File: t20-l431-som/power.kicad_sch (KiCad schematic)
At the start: 21 parts, among them U1 STM32L431-WLCSP64, U2 T20W80

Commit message: Continued initial work on t20-l431 som
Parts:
- added C18: 1 uF, azonenberg_pcb:EIA_0201_CAP_NOSILK, symbol device:C
- C1, C10, C11, C12, C13, C14, C15, C16, C17, C2, C3, C4, C5, C6, C7, C8, C9, L1, L2: footprint (none) -> azonenberg_pcb:EIA_0201_CAP_NOSILK
- U1: footprint (none) -> azonenberg_pcb:BGA_64_0.35MM_3p1MM_STM32L431
- U2: footprint (none) -> azonenberg_pcb:BGA_80_0.4MM_4p4x3p5_T20W80
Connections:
- net A1V2_PLL: now also C18.1
- net GND: now also C18.2
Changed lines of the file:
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@@
 	(generator "eeschema")
 	(generator_version "9.0")
-	(paper "A3")
+	(paper "A4")
 	(text "TODO: LDOs"
 		(exclude_from_sim no)
@@
 	)
 	(junction
+		(at 92.71 99.06)
+		(diameter 0)
+		(color 0 0 0 0)
+	)
+	(junction
 		(at 26.67 30.48)
 		(diameter 0)
@@
 	(wire
 		(pts
+			(xy 92.71 99.06) (xy 105.41 99.06)
+		)
+		(stroke
+			(width 0)
+			(type default)
+		)
+	)
+	(wire
+		(pts
 			(xy 26.67 76.2) (xy 26.67 78.74)
 		)
@@
 		(pts
 			(xy 26.67 78.74) (xy 26.67 81.28)
+		)
+		(stroke
+			(width 0)
+			(type default)
+		)
+	)
+	(wire
+		(pts
+			(xy 92.71 106.68) (xy 105.41 106.68)
 		)
 		(stroke
@@
 			)
 			(justify right bottom)
+		)
+	)
+	(hierarchical_label "1V8"
+		(shape output)
+		(at 151.13 64.77 0)
+		(effects
+			(font
+				(size 1.27 1.27)
+			)
+			(justify left)
 		)
 	)
@@
 			)
 		)
-		(property "Footprint" ""
+		(property "Footprint" "azonenberg_pcb:EIA_0201_CAP_NOSILK"
 			(at 60.6552 67.31 0)
 			(effects
@@
 			)
 		)
-		(property "Footprint" ""
+		(property "Footprint" "azonenberg_pcb:BGA_64_0.35MM_3p1MM_STM32L431"
 			(at 30.48 49.53 0)
 			(effects
@@
 			)
 		)
-		(property "Footprint" ""
+		(property "Footprint" "azonenberg_pcb:EIA_0201_CAP_NOSILK"
 			(at 74.6252 67.31 0)
 			(effects
@@
 			)
 		)
-		(property "Footprint" ""
+		(property "Footprint" "azonenberg_pcb:EIA_0201_CAP_NOSILK"
 			(at 117.8052 81.28 0)
 			(effects
@@
 			)
 		)
-		(property "Footprint" ""
+		(property "Footprint" "azonenberg_pcb:EIA_0201_CAP_NOSILK"
 			(at 86.0552 67.31 0)
 			(effects
@@
 			)
 		)
-		(property "Footprint" ""
+		(property "Footprint" "azonenberg_pcb:EIA_0201_CAP_NOSILK"
 			(at 83.5152 46.99 0)
 			(effects
@@
 			)
 		)
-		(property "Footprint" ""
+		(property "Footprint" "azonenberg_pcb:EIA_0201_CAP_NOSILK"
 			(at 60.6552 81.28 0)
 			(effects
@@
 			)
 		)
-		(property "Footprint" ""
+		(property "Footprint" "azonenberg_pcb:EIA_0201_CAP_NOSILK"
 			(at 94.9452 81.28 0)
 			(effects
@@
 			)
 		)
-		(property "Footprint" ""
+		(property "Footprint" "azonenberg_pcb:EIA_0201_CAP_NOSILK"
 			(at 83.5152 81.28 0)
 			(effects
@@
 			)
 		)
-		(property "Footprint" ""
+		(property "Footprint" "azonenberg_pcb:EIA_0201_CAP_NOSILK"
 			(at 60.6552 93.98 0)
 			(effects
@@
 			)
 		)
-		(property "Footprint" ""
+		(property "Footprint" "azonenberg_pcb:BGA_80_0.4MM_4p4x3p5_T20W80"
 			(at 30.48 125.73 0)
 			(effects
@@
 				(path "/c9028163-a5a7-4e78-bba9-fb79df7846cd/cee616b2-310c-4168-8c64-88604d0390f4"
 					(reference "U2")
+					(unit 1)
+				)
+			)
+		)
+	)
+	(symbol
+		(lib_id "device:C")
+		(at 105.41 102.87 0)
+		(unit 1)
+		(exclude_from_sim no)
+		(in_bom yes)
+		(on_board yes)
+		(dnp no)
+		(fields_autoplaced yes)
+		(property "Reference" "C18"
+			(at 108.331 101.6578 0)
+			(effects
+				(font
+					(size 1.27 1.27)
+				)
+				(justify left)
+			)
+		)
+		(property "Value" "1 uF"
+			(at 108.331 104.0821 0)
+			(effects
+				(font
+					(size 1.27 1.27)
+				)
+				(justify left)
+			)
+		)
+		(property "Footprint" "azonenberg_pcb:EIA_0201_CAP_NOSILK"
+			(at 106.3752 106.68 0)
+			(effects
+				(font
+					(size 1.27 1.27)
+				)
+				(hide yes)
+			)
+		)
+		(property "Datasheet" ""
+			(at 105.41 102.87 0)
+			(effects
+				(font
+					(size 1.27 1.27)
+				)
+				(hide yes)
+			)
+		)
+		(property "Description" "Unpolarized capacitor"
+			(at 105.41 102.87 0)
+			(effects
+				(font
+					(size 1.27 1.27)
+				)
+				(hide yes)
+			)
+		)
+		(property "MPN" "GRM033C80J105ME05D"
+			(at 105.41 102.87 0)
+			(effects
+				(font
+					(size 1.27 1.27)
+				)
+				(hide yes)
+			)
+		)
+		(pin "2"
+		)
+		(pin "1"
+		)
+		(instances
+			(project "t20-l431-som"
+				(path "/c9028163-a5a7-4e78-bba9-fb79df7846cd/cee616b2-310c-4168-8c64-88604d0390f4"
+					(reference "C18")
 					(unit 1)
 				)
@@
 			)
 		)
-		(property "Footprint" ""
+		(property "Footprint" "azonenberg_pcb:EIA_0201_CAP_NOSILK"
 			(at 76.2 99.06 0)
 			(effects
@@
 					(size 1.524 1.524)
 				)
+				(hide yes)
 			)
 		)
@@
 			)
 		)
-		(property "Footprint" ""
+		(property "Footprint" "azonenberg_pcb:EIA_0201_CAP_NOSILK"
 			(at 72.0852 81.28 0)
 			(effects
@@
 			)
 		)
-		(property "Footprint" ""
+		(property "Footprint" "azonenberg_pcb:EIA_0201_CAP_NOSILK"
 			(at 97.4852 67.31 0)
 			(effects
@@
 			)
 		)
-		(property "Footprint" ""
+		(property "Footprint" "azonenberg_pcb:EIA_0201_CAP_NOSILK"
 			(at 72.0852 46.99 0)
 			(effects
@@
 			)
 		)
-		(property "Footprint" ""
+		(property "Footprint" "azonenberg_pcb:EIA_0201_CAP_NOSILK"
 			(at 106.3752 81.28 0)
 			(effects
@@
 			)
 		)
-		(property "Footprint" ""
+		(property "Footprint" "azonenberg_pcb:EIA_0201_CAP_NOSILK"
 			(at 93.6752 34.29 0)
 			(effects
@@
 			)
 		)
-		(property "Footprint" ""
+		(property "Footprint" "azonenberg_pcb:EIA_0201_CAP_NOSILK"
 			(at 93.6752 106.68 0)
 			(effects
@@
 			)
 		)
-		(property "Footprint" ""
+		(property "Footprint" "azonenberg_pcb:EIA_0201_CAP_NOSILK"
 			(at 93.6752 46.99 0)
 			(effects
@@
 			)
 		)
-		(property "Footprint" ""
+		(property "Footprint" "azonenberg_pcb:EIA_0201_CAP_NOSILK"
 			(at 60.6552 46.99 0)
 			(effects
@@
 			)
 		)
-		(property "Footprint" ""
+		(property "Footprint" "azonenberg_pcb:EIA_0201_CAP_NOSILK"
 			(at 76.2 26.67 0)
 			(effects
@@
 					(size 1.524 1.524)
 				)
-			)
-		)
+				(hide yes)
+			)
+		)

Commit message: Continued initial layout
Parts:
- added C20: 0.01 uF, azonenberg_pcb:EIA_0201_CAP_NOSILK, symbol device:C
- added C21, C22, C23: 1 uF, azonenberg_pcb:EIA_0201_CAP_NOSILK, symbol device:C
- added R2, R3: 10K, azonenberg_pcb:EIA_0201_RES_NOSILK, symbol device:R
- added U4: MODULE_INTERNAL_T20_L431_HOST, azonenberg_pcb:MODULE_INTERNAL_T20_L431_HOST, symbol special-azonenberg:MODULE_INTERNAL_T20_L431_HOST
- added U5: LP3986TL-2518/NOPB, azonenberg_pcb:BGA_8_0.5MM_1.6MM_TI_YZR0008, symbol power-azonenberg:LP3986
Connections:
- net 1V2: now also U4.C2 (1V2), U4.C3 (1V2), U4.D2 (1V2), U4.E2 (1V2), U4.F2 (1V2), U4.G4 (1V2)
- net 1V8: now also C21.1, U5.A1 (VOUT2)
- net 2V5: now also C22.1, U4.C4 (2V5), U5.A3 (VOUT1)
- net 3V3: now also C23.1, U4.G11 (3V3), U5.A2 (VIN); no longer C7.1, C8.1, C9.1, U2.F6 (VCCIO3A_3B_3C), U2.G3 (VCCIO1B_1C_1D_1E), U2.G5 (VCCIO3D_3E_4A_4B)
- net GND: now also C20.2, C21.2, C22.2, C23.2, R2.2, R3.2, U4.A3 (GND), U4.B3 (GND), U4.D4 (GND), U4.D5 (GND), U4.G10 (GND), U4.G12 (GND), U4.G8 (GND), U5.C2 (GND), U5.C3 (GND)
- new net: C20.1, U5.C1 (BYPASS)
- new net 1V8_EN: R3.1, U5.B1 (EN2)
- new net 2V5_EN: R2.1, U5.B3 (EN1)
- new net 3V3_FPGA: C7.1, C8.1, C9.1, U2.F6 (VCCIO3A_3B_3C), U2.G3 (VCCIO1B_1C_1D_1E), U2.G5 (VCCIO3D_3E_4A_4B), U4.C6 (3V3_FPGA), U4.D6 (3V3_FPGA)
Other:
- note added: "!!!!! External 4.7 uF bulk cap required on host board"
- note added: "TODO: LDO for Vcore"
- note added: "TODO: need separate switched 3V3 rail for the FPGA??"
- note added: "We probably dont need output caps at the LDO since we have so much at the FPGA/MCU right there But whatever, they're small"
- note removed: "TODO: LDOs"

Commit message: Continued initial layout
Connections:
- net 3V3: now also U4.J4 (3V3)
- net GND: now also U4.C1 (GND), U4.D1 (GND), U4.E1 (GND), U4.F1 (GND), U4.F3 (GND), U4.F8 (GND), U4.J3 (GND), U4.J6 (GND)
- net VBAT: now also U4.N3 (VBAT)

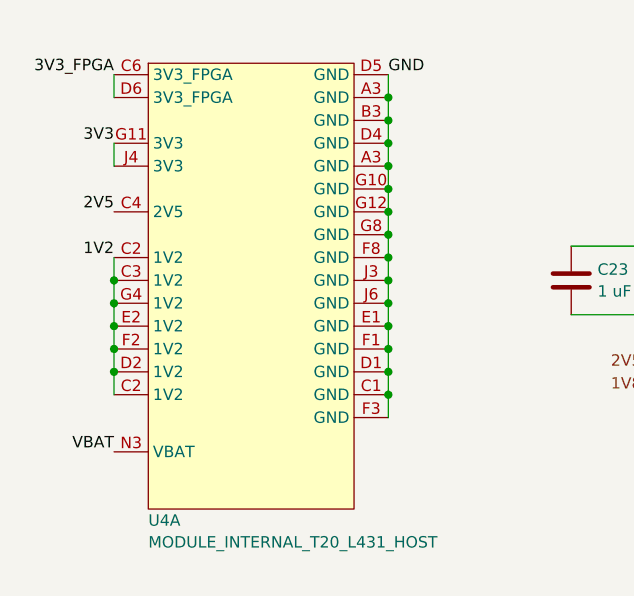
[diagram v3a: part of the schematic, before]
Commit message: Continued STM32 fanout
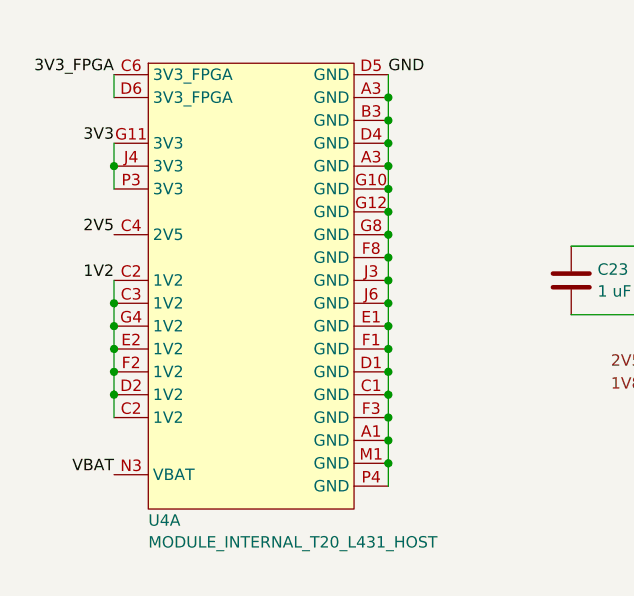
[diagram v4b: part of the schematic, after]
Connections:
- net 3V3: now also U4.P3 (3V3)
- net GND: now also U4.A1 (GND), U4.M1 (GND), U4.P4 (GND)

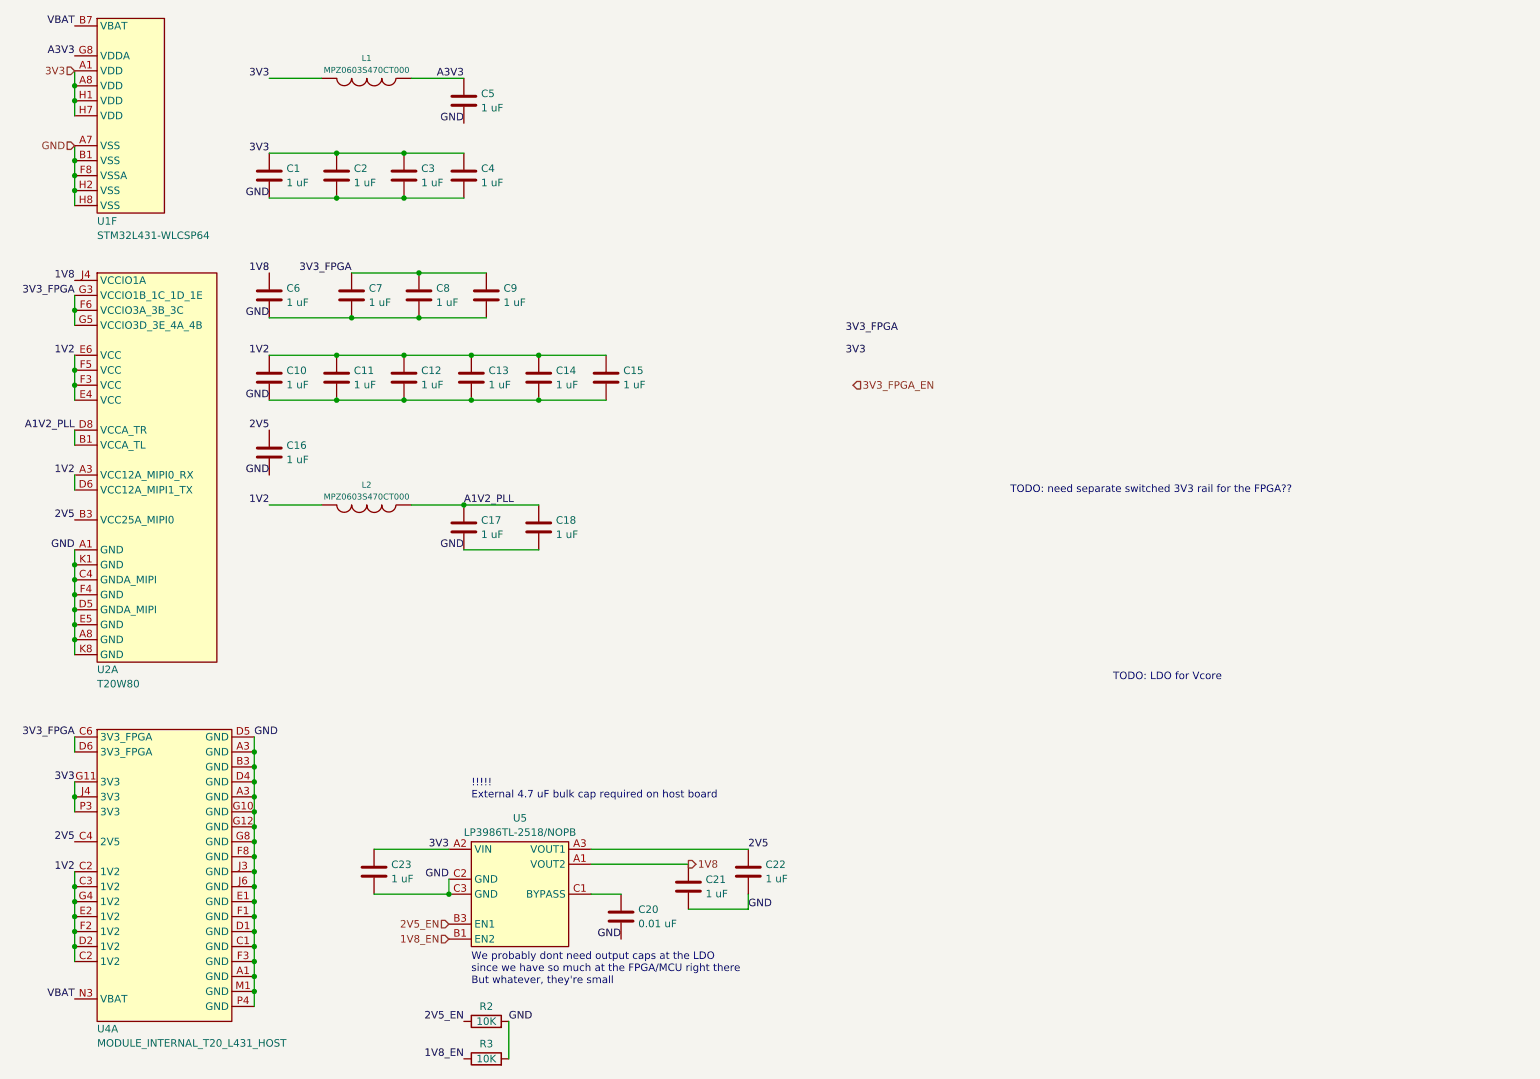
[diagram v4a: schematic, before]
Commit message: Added oscillator
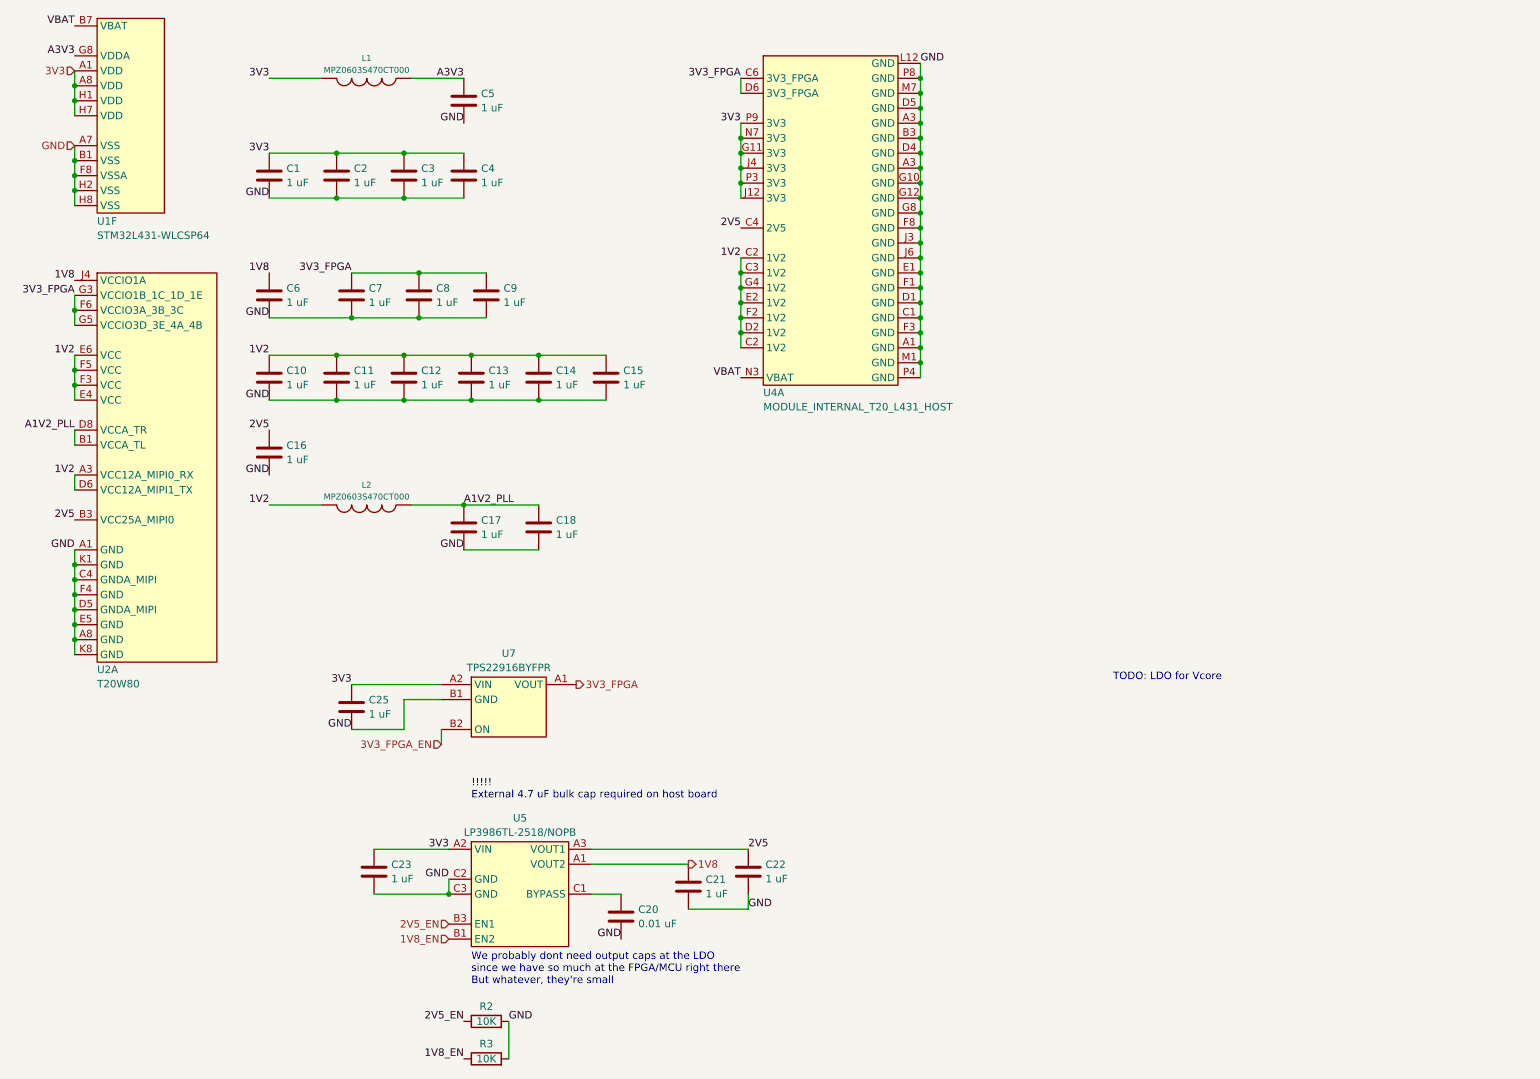
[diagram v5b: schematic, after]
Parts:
- added C25: 1 uF, azonenberg_pcb:EIA_0201_CAP_NOSILK, symbol device:C
- added U7: TPS22916BYFPR, azonenberg_pcb:BGA_4_0.4MM_0.8x0.8_TI_YFP0004, symbol power-azonenberg:TPS22916BYFPR
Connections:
- net 3V3: now also U4.J12 (3V3), U4.N7 (3V3), U4.P9 (3V3), C25.1, U7.A2 (VIN)
- net 3V3_FPGA: now also U7.A1 (VOUT)
- net 3V3_FPGA_EN: now also U7.B2 (ON)
- net GND: now also U4.L12 (GND), U4.M7 (GND), U4.P8 (GND), C25.2, U7.B1 (GND)
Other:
- note removed: "TODO: need separate switched 3V3 rail for the FPGA??"

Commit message: Finished initial L431 SOM routing
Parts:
- added C27, C28: 1 uF, azonenberg_pcb:EIA_0201_CAP_NOSILK, symbol device:C
- added C29, C30, C31: 4.7 uF 2.5V, azonenberg_pcb:EIA_0201_CAP_NOSILK, symbol device:C
- added R8, R9: 10K, azonenberg_pcb:EIA_0201_RES_NOSILK, symbol device:R
- added U9: NCP139AFCT120T2G, azonenberg_pcb:BGA_6_1.3x1.0_0.4MM, symbol power-azonenberg:NCP139
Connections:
- net 1V2: now also C29.1, C30.1, C31.1, U9.A1 (VOUT), U9.B1 (SNS/FB)
- net 3V3: now also U4.L8 (3V3), U4.P10 (3V3), U4.P8 (3V3), C27.1, C28.1, U9.A2 (VIN), U9.C2 (BIAS); no longer U4.P9 (3V3)
- net 3V3_FPGA_EN: now also R8.1
- net GND: now also U4.B9 (GND), U4.C9 (GND), U4.M10 (GND), U4.M9 (GND), U4.P9 (GND), C27.2, C28.2, C29.2, C30.2, C31.2, R8.2, R9.2, U9.C1 (GND); no longer U4.P8 (GND)
- new net 1V2_EN: R9.1, U9.B2 (EN)
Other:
- note added: "!!!!! External 2x 4.7 uF bulk cap required on host board for 3.3V rail"
- note removed: "!!!!! External 4.7 uF bulk cap required on host board"
- note removed: "TODO: LDO for Vcore"

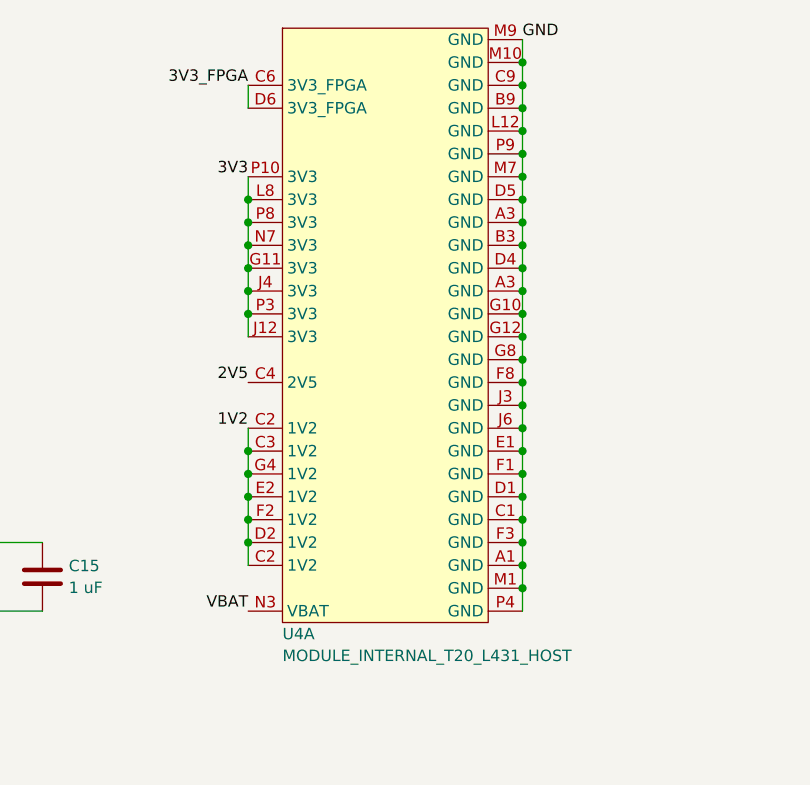
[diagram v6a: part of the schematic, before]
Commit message: Continued L431 SoM layout
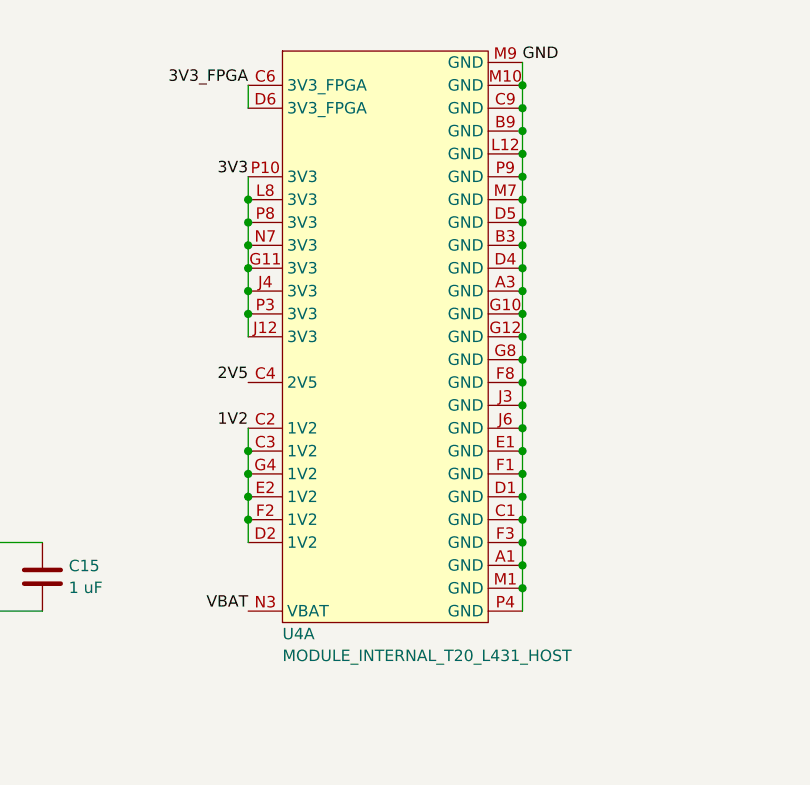
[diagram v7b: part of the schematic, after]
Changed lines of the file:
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@@
 	)
 	(junction
-		(at 139.7 73.66)
-		(diameter 0)
-		(color 0 0 0 0)
-	)
-	(junction
 		(at 105.41 81.28)
 		(diameter 0)
@@
 	)
 	(junction
-		(at 170.18 20.32)
-		(diameter 0)
-		(color 0 0 0 0)
-	)
-	(junction
 		(at 71.12 46.99)
 		(diameter 0)
@@
 	(wire
 		(pts
-			(xy 170.18 17.78) (xy 170.18 20.32)
-		)
-		(stroke
-			(width 0)
-			(type default)
-		)
-	)
-	(wire
-		(pts
 			(xy 170.18 22.86) (xy 170.18 25.4)
 		)
@@
 	(wire
 		(pts
-			(xy 139.7 73.66) (xy 139.7 76.2)
-		)
-		(stroke
-			(width 0)
-			(type default)
-		)
-	)
-	(wire
-		(pts
 			(xy 114.3 160.02) (xy 130.81 160.02)
 		)
@@
 	)
 	(label "GND"
-		(at 170.18 17.78 0)
+		(at 170.18 20.32 0)
 		(effects
 			(font
@@
 		(pin "D2"
 		)
-		(pin "C2"
-		)
-		(pin "A3"
+		(pin "P2"
 		)
 		(pin "E8"
@@
 		(pin "P3"
 		)
-		(pin "P2"
+		(pin "R1"
 		)
 		(pin "N2"
@@
 		(pin "K2"
 		)
-		(pin "R1"
+		(pin "R3"
 		)
 		(pin "R2"
 		)
-		(pin "R3"
+		(pin "R6"
 		)
 		(pin "J7"
@@
 		(pin "M7"
 		)
-		(pin "M7"
+		(pin "L9"
 		)
 		(pin "P5"
@@
 		(pin "R4"
 		)
-		(pin "R7"
+		(pin "P7"
 		)
 		(pin "P6"
 		)
-		(pin "R6"
+		(pin "R7"
 		)
 		(pin "N8"
@@
 		(pin "L8"
 		)
-		(pin "~"
-		)
 		(pin "P10"
